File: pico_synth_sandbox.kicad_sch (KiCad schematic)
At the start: 22 parts, among them J1 Micro_SD_Card_Det2, SW1 RotaryEncoder_Switch, SW2 RotaryEncoder_Switch, SW3 PWR_EN, U1 Pico, U2 MIC5219-3.3YM5

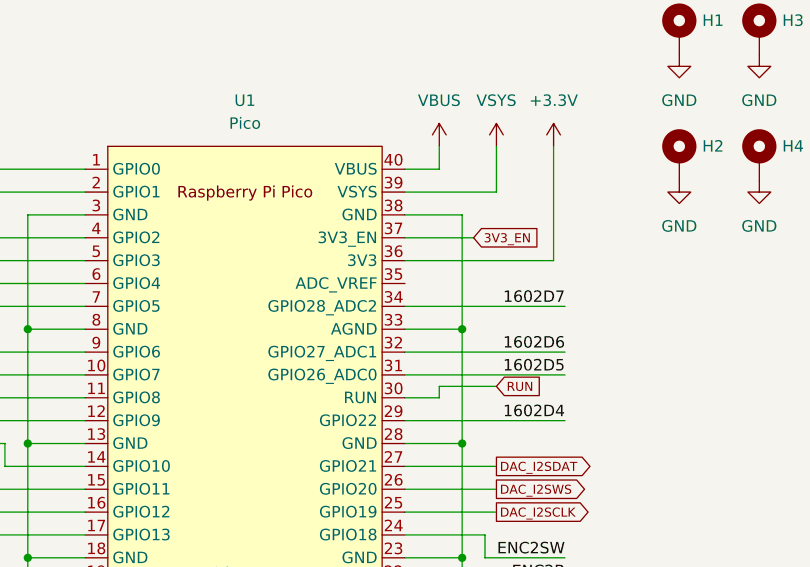
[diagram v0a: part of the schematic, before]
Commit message: Minor update to ADC connection.
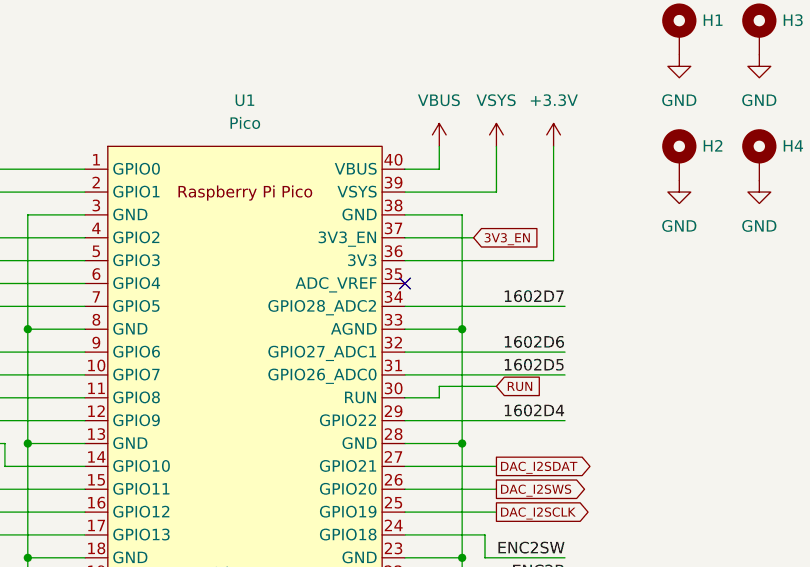
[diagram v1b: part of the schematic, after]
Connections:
- no-connect marks 7 -> 8
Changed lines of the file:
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@@
   )
   (no_connect (at 49.53 168.91))
+  (no_connect (at 88.9 62.23))
   (no_connect (at 49.53 166.37))
   (no_connect (at 49.53 161.29))
